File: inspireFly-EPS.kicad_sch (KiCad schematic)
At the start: 24 parts, among them J1 USB4085-GF-A_REVB, Q3 NMOS, Q4 NMOS, U1 STM32U575RIT6, U2 BQ25750RRVR, U3 TCAN332DCNR

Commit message: Good progress on BQ chip - need to do math later
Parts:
- added C14, C17: 80uF, symbol Device:C
- added C15, C16: 47nF, symbol Device:C
- added C18, C19: 100nF, symbol Device:C
- added C20: 470nF, symbol Device:C
- added C21, C22: 4.7uF, symbol Device:C
- added L1: L, symbol Device:L
- added Q10, Q5, Q6, Q7, Q8, Q9: NMOS, symbol Simulation_SPICE:NMOS
- added R10: 5.24k, symbol Device:R_US
- added R11: 30.31k, symbol Device:R_US
- added R12: 80k, symbol Device:R_US
- added R13: 3.3k, symbol Device:R_US
- added R14: 4.2k, symbol Device:R_US
- added R5: 5m, symbol Device:R_US
- added R6, R7: 10, symbol Device:R_US
- added R8: 250k, symbol Device:R_US
- added R9: 12k, symbol Device:R_US
- added TH1: Thermistor_US, symbol Device:Thermistor_US
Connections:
- net GND: now also U2.37 (EPAD), U2.8 (TS), C14.2, C17.2, C18.2, C19.1, C22.1, Q6.3 (S), Q8.3 (S), R10.2, R11.1, R11.2, R12.2, R13.1, R14.1, TH1.1, TH1.2
- net V_PROTECTED: now reaches R1.2, R3.1, R4.1
- net V_PROTECTED: now also U2.32 (SYS), C14.1, Q5.1 (D), Q9.1 (D)
- net at U2.10 (ILIM_HIZ): now also R13.2
- net at U2.11 (FBG): now also R9.2
- net at U2.12 (FB): now also R8.2, R9.1
- net at U2.13 (SRN): now also C19.2, C20.1, R7.1
- net at U2.14 (SRP): now also C18.1, C20.2, R6.1
- net at U2.15 (BATDRV): now also Q10.2 (G), Q9.2 (G)
- net at U2.16 (BATSRC): now also Q10.1 (D), Q9.3 (S)
- net at U2.18 (SW2): now also C16.2, L1.2, Q7.3 (S), Q8.1 (D)
- net at U2.19 (HIDRV2): now also Q7.2 (G)
- net at U2.20 (BTST2): now also C16.1
- net at U2.21 (LODRV2): now also Q8.2 (G)
- net +5V: now reaches U2.23 (DRV_SUP)
- net +5V: now also C22.2
- net at U2.24 (REGN): now also C21.1
- net at U2.25 (LODRV1): now also Q6.2 (G)
- net at U2.26 (BTST1): now also C15.1
- net at U2.27 (HIDRV1): now also Q5.2 (G)
- net at U2.28 (SW1): now also C15.2, L1.1, Q5.3 (S), Q6.1 (D)
- net at U2.36 (FSW_SYNC): now also R12.1
- net at U2.9 (ICHG): now also R14.2
- new net: C17.1, Q10.3 (S), Q7.1 (D), R5.1, R6.2
- new net BAT +: R5.2, R7.2, R8.1
- new net REGEN: C21.2, R10.1
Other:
- moved on the sheet: C10, C11, C12, C13, Q3, Q4, R1, R2, R3, R4, U2

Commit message: Changes to BQ Chip
Calculated some values, see overleaf doc. Adjusted presentation on schematic in regards to BQ chip. Also added battery holders
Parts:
- added BT1, BT2: BK-18650-PC4, BK-18650-PC4:BAT_BK-18650-PC4, symbol InspireFly-EPS-sym_lib:BK-18650-PC4
- added C23: ~, symbol Device:C
- added R15: 22.5k, symbol Device:R_US
- added R16: 1M, symbol Device:R_US
- added R17: 100k, symbol Device:R_US
- R8: value 250k -> 200k
- R9: value 12k -> 44.8k
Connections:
- net BAT +: now also BT1.1+, BT1.2+
- net GND: now also BT2.1-, BT2.2-, C23.2, R15.2; no longer U2.35 (ACOV)
- net V_BUS_COMBINED: now also C23.1, R16.1; no longer U2.34 (ACUV)
- net at C19.2, C20.1, R7.1: now also U2.14 (SRP); no longer U2.13 (SRN)
- net at C18.1, C20.2, R6.1: now also U2.13 (SRN); no longer U2.14 (SRP)
- new net: R15.1, R17.2, U2.35 (ACOV)
- new net: R16.2, R17.1, U2.34 (ACUV)
- new net: BT1.1-, BT1.2-, BT2.1+, BT2.2+
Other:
- moved on the sheet: C10, C11, C12, C13, C14, C15, C16, C17, C18, C19, C20, C21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

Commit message: More BQ work
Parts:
- L1: value L -> 2.2uH
- R1: value 2m -> 5m
- R12: value 80k -> 40k
- R14: value 4.2k -> 12.5k
- R15: value 22.5k -> 22.6k
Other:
- moved on the sheet: C13, C14
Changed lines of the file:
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@@
 	)
 	(junction
-		(at 347.98 261.62)
-		(diameter 0)
-		(color 0 0 0 0)
-	)
-	(junction
 		(at 250.19 91.44)
 		(diameter 0)
@@
 	)
 	(junction
-		(at 358.14 261.62)
-		(diameter 0)
-		(color 0 0 0 0)
-	)
-	(junction
 		(at 261.62 86.36)
 		(diameter 0)
@@
 	)
 	(junction
+		(at 349.25 261.62)
+		(diameter 0)
+		(color 0 0 0 0)
+	)
+	(junction
 		(at 260.35 91.44)
 		(diameter 0)
@@
 	)
 	(junction
+		(at 360.68 261.62)
+		(diameter 0)
+		(color 0 0 0 0)
+	)
+	(junction
 		(at 248.92 71.12)
 		(diameter 0)
@@
 	(wire
 		(pts
-			(xy 347.98 288.29) (xy 349.25 288.29)
-		)
-		(stroke
-			(width 0)
-			(type default)
-		)
-	)
-	(wire
-		(pts
 			(xy 124.46 317.5) (xy 124.46 323.85)
 		)
@@
 	(wire
 		(pts
-			(xy 327.66 276.86) (xy 327.66 279.4)
+			(xy 326.39 273.05) (xy 326.39 279.4)
 		)
 		(stroke
@@
 	(wire
 		(pts
-			(xy 347.98 288.29) (xy 347.98 261.62)
+			(xy 349.25 288.29) (xy 349.25 261.62)
 		)
 		(stroke
@@
 	(wire
 		(pts
-			(xy 347.98 261.62) (xy 358.14 261.62)
-		)
-		(stroke
-			(width 0)
-			(type default)
-		)
-	)
-	(wire
-		(pts
 			(xy 38.1 210.82) (xy 38.1 213.36)
 		)
@@
 	(wire
 		(pts
-			(xy 326.39 273.05) (xy 326.39 276.86)
-		)
-		(stroke
-			(width 0)
-			(type default)
-		)
-	)
-	(wire
-		(pts
 			(xy 318.77 302.26) (xy 312.42 302.26)
 		)
@@
 	(wire
 		(pts
+			(xy 349.25 261.62) (xy 360.68 261.62)
+		)
+		(stroke
+			(width 0)
+			(type default)
+		)
+	)
+	(wire
+		(pts
 			(xy 270.51 93.98) (xy 274.32 93.98)
 		)
@@
 	(wire
 		(pts
-			(xy 358.14 273.05) (xy 358.14 275.59)
+			(xy 360.68 273.05) (xy 360.68 276.86)
 		)
 		(stroke
@@
 	(wire
 		(pts
-			(xy 359.41 275.59) (xy 359.41 276.86)
-		)
-		(stroke
-			(width 0)
-			(type default)
-		)
-	)
-	(wire
-		(pts
 			(xy 257.81 68.58) (xy 274.32 68.58)
 		)
@@
 	(wire
 		(pts
-			(xy 358.14 275.59) (xy 359.41 275.59)
-		)
-		(stroke
-			(width 0)
-			(type default)
-		)
-	)
-	(wire
-		(pts
 			(xy 308.61 132.08) (xy 312.42 132.08)
 		)
@@
 	(wire
 		(pts
-			(xy 326.39 276.86) (xy 327.66 276.86)
-		)
-		(stroke
-			(width 0)
-			(type default)
-		)
-	)
-	(wire
-		(pts
 			(xy 236.22 86.36) (xy 248.92 86.36)
 		)
@@
 	(wire
 		(pts
-			(xy 358.14 261.62) (xy 372.11 261.62)
-		)
-		(stroke
-			(width 0)
-			(type default)
-		)
-	)
-	(wire
-		(pts
 			(xy 251.46 297.18) (xy 331.47 297.18)
 		)
@@
 	(wire
 		(pts
-			(xy 358.14 261.62) (xy 358.14 265.43)
+			(xy 360.68 261.62) (xy 360.68 265.43)
 		)
 		(stroke
@@
 	(wire
 		(pts
-			(xy 326.39 261.62) (xy 347.98 261.62)
+			(xy 326.39 261.62) (xy 349.25 261.62)
 		)
 		(stroke
@@
 	(wire
 		(pts
+			(xy 360.68 261.62) (xy 372.11 261.62)
+		)
+		(stroke
+			(width 0)
+			(type default)
+		)
+	)
+	(wire
+		(pts
 			(xy 276.86 317.5) (xy 261.62 317.5)
 		)
@@
 	(symbol
 		(lib_id "power:GND")
-		(at 327.66 287.02 0)
+		(at 326.39 287.02 0)
 		(unit 1)
 		(exclude_from_sim no)
@@
 		(fields_autoplaced yes)
 		(property "Reference" "#PWR016"
-			(at 327.66 293.37 0)
+			(at 326.39 293.37 0)
 			(effects
 				(font
@@
 		)
 		(property "Value" "GND"
-			(at 327.66 292.1 0)
+			(at 326.39 292.1 0)
 			(effects
 				(font
@@
 		)
 		(property "Footprint" ""
-			(at 327.66 287.02 0)
+			(at 326.39 287.02 0)
 			(effects
 				(font
@@
 		)
 		(property "Datasheet" ""
-			(at 327.66 287.02 0)
+			(at 326.39 287.02 0)
 			(effects
 				(font
@@
 		)
 		(property "Description" "Power symbol creates a global label with name \"GND\" , ground"
-			(at 327.66 287.02 0)
+			(at 326.39 287.02 0)
 			(effects
 				(font
@@
 	(symbol
 		(lib_id "Device:C")
-		(at 358.14 269.24 0)
+		(at 360.68 269.24 0)
 		(unit 1)
 		(exclude_from_sim no)
@@
 		(fields_autoplaced yes)
 		(property "Reference" "C14"
-			(at 361.95 267.9699 0)
+			(at 364.49 267.9699 0)
 			(effects
 				(font
@@
 		)
 		(property "Value" "80uF"
-			(at 361.95 270.5099 0)
+			(at 364.49 270.5099 0)
 			(effects
 				(font
@@
 		)
 		(property "Footprint" ""
-			(at 359.1052 273.05 0)
+			(at 361.6452 273.05 0)
 			(effects
 				(font
@@
 		)
 		(property "Datasheet" "~"
-			(at 358.14 269.24 0)
+			(at 360.68 269.24 0)
 			(effects
 				(font
@@
 		)
 		(property "Description" "Unpolarized capacitor"
-			(at 358.14 269.24 0)
+			(at 360.68 269.24 0)
 			(effects
 				(font
@@
 			)
 		)
-		(property "Value" "80k"
+		(property "Value" "40k"
 			(at 258.318 284.988 90)
 			(effects
@@
 			)
 		)
-		(property "Value" "22.5k"
+		(property "Value" "22.6k"
 			(at 275.59 287.0199 0)
 			(effects
@@
 			)
 		)
-		(property "Value" "2m"
+		(property "Value" "5m"
 			(at 307.34 257.81 90)
 			(effects
@@
 	(symbol
 		(lib_id "power:GND")
-		(at 359.41 276.86 0)
+		(at 360.68 276.86 0)
 		(unit 1)
 		(exclude_from_sim no)
@@
 		(fields_autoplaced yes)
 		(property "Reference" "#PWR019"
-			(at 359.41 283.21 0)
+			(at 360.68 283.21 0)
 			(effects
 				(font
@@
 		)
 		(property "Value" "GND"
-			(at 359.41 281.94 0)
+			(at 360.68 281.94 0)
 			(effects
 				(font
@@
 		)
 		(property "Footprint" ""
-			(at 359.41 276.86 0)
+			(at 360.68 276.86 0)
 			(effects
 				(font
@@
 		)
 		(property "Datasheet" ""
-			(at 359.41 276.86 0)
+			(at 360.68 276.86 0)
 			(effects
 				(font
@@
 		)
 		(property "Description" "Power symbol creates a global label with name \"GND\" , ground"
-			(at 359.41 276.86 0)
+			(at 360.68 276.86 0)
 			(effects
 				(font
@@
 			)
 		)
-		(property "Value" "4.2k"
+		(property "Value" "12.5k"
 			(at 190.754 303.784 90)
 			(effects
@@
 			)
 		)
-		(property "Value" "L"
+		(property "Value" "2.2uH"
 			(at 361.95 299.72 90)
 			(effects
@@
 	(symbol
 		(lib_id "Device:C")
-		(at 327.66 283.21 0)
+		(at 326.39 283.21 0)
 		(unit 1)
 		(exclude_from_sim no)
@@
 		(fields_autoplaced yes)
 		(property "Reference" "C13"
-			(at 331.47 281.9399 0)
+			(at 330.2 281.9399 0)
 			(effects
 				(font
@@
 		)
 		(property "Value" "2.2uF"
-			(at 331.47 284.4799 0)
+			(at 330.2 284.4799 0)
 			(effects
 				(font
@@
 		)
 		(property "Footprint" ""
-			(at 328.6252 287.02 0)
+			(at 327.3552 287.02 0)
 			(effects
 				(font
@@
 		)
 		(property "Datasheet" "~"
-			(at 327.66 283.21 0)
+			(at 326.39 283.21 0)
 			(effects
 				(font
@@
 		)
 		(property "Description" "Unpolarized capacitor"
-			(at 327.66 283.21 0)
+			(at 326.39 283.21 0)
 			(effects
 				(font

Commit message: Updates to BQ chip and routing
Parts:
- added D1: LED, Diode_SMD:D_0805_2012Metric_Pad1.15x1.40mm_HandSolder, symbol Device:LED
- added J2: Conn_01x02_Pin, Connector_PinSocket_2.54mm:PinSocket_1x02_P2.54mm_Vertical, symbol Connector:Conn_01x02_Pin
- added R18, R19: 10k, Resistor_SMD:R_0402_1005Metric_Pad0.72x0.64mm_HandSolder, symbol Device:R_US
- added R20: 330, Resistor_SMD:R_0402_1005Metric_Pad0.72x0.64mm_HandSolder, symbol Device:R_US
- added R21: 10K, Resistor_SMD:R_0402_1005Metric_Pad0.72x0.64mm_HandSolder, symbol Device:R_US
- BT1, BT2: footprint BK-18650-PC4:BAT_BK-18650-PC4 -> inspireFly-EPS-footprints:BAT_BK-18650-PC4
- C1, C13, C15, C16, C18, C19, C2, C20, C21, C22, C3, C4, C5, C6, C7, C8, C9: footprint (none) -> Capacitor_SMD:C_0402_1005Metric_Pad0.74x0.62mm_HandSolder
- C10, C11: footprint (none) -> Capacitor_SMD:C_0805_2012Metric_Pad1.18x1.45mm_HandSolder
- C12: footprint (none) -> Capacitor_SMD:C_1206_3216Metric_Pad1.33x1.80mm_HandSolder
- C14, C17: value 80uF -> 47uF; footprint (none) -> inspireFly-EPS-footprints:CAP_EEEFN1J470L
- C23: value ~ -> 2.2uF; footprint (none) -> Capacitor_SMD:C_1206_3216Metric_Pad1.33x1.80mm_HandSolder
- J1: footprint USB4085-GF-A_REVB:GCT_USB4085-GF-A_REVB -> inspireFly-EPS-footprints:GCT_USB4085-GF-A_REVB
- L1: footprint (none) -> inspireFly-EPS-footprints:WE-MXGI_4020
- Q10, Q3, Q4, Q5, Q6, Q7, Q8, Q9: value NMOS -> SQJA62EP-T1_GE3; footprint (none) -> inspireFly-EPS-footprints:TRANS_SQJA62EP-T1_GE3
- R1, R4, R5: footprint (none) -> Resistor_SMD:R_1206_3216Metric_Pad1.30x1.75mm_HandSolder
- R10, R11, R12, R13, R14, R15, R16, R17, R8, R9, TR1: footprint (none) -> Resistor_SMD:R_0402_1005Metric_Pad0.72x0.64mm_HandSolder
- R2, R3, R6, R7: footprint (none) -> Resistor_SMD:R_0603_1608Metric_Pad0.98x0.95mm_HandSolder
- U1: footprint LQFP64-10x10mm_STM -> inspireFly-EPS-footprints:LQFP64-10x10mm_STM
- U2: footprint VQFN36_RRV_TEX -> inspireFly-EPS-footprints:VQFN36_RRV_TEX
- U3: footprint DCN0008A_N -> Package_TO_SOT_SMD:SOT-23-8
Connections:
- net V_BUS_COMBINED is gone; now on net USB_V: C23.1, Q3.1 (D), R16.1, U2.33 (VAC)
- net +3.3V: now also R18.2, R19.2, R21.1
- net GND: now also U2.7 (*CE), D1.1 (K), J2.2 (Pin_2)
- net USB_V: now also J2.1 (Pin_1)
- net I2C3-SCL: now reaches U1.8 (PC0)
- net I2C3-SCL: now also U2.2 (SDA), R18.1
- net I2C3-SDA: now reaches U1.9 (PC1)
- net I2C3-SDA: now also U2.1 (SCL), R19.1
- net POWER_GOOD: now reaches U2.6 (*PG)
- net POWER_GOOD: now also R20.1, R21.2
- new net: D1.2 (A), R20.2
- no-connect marks 6 -> 9
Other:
- moved on the sheet: C12, C14, C17

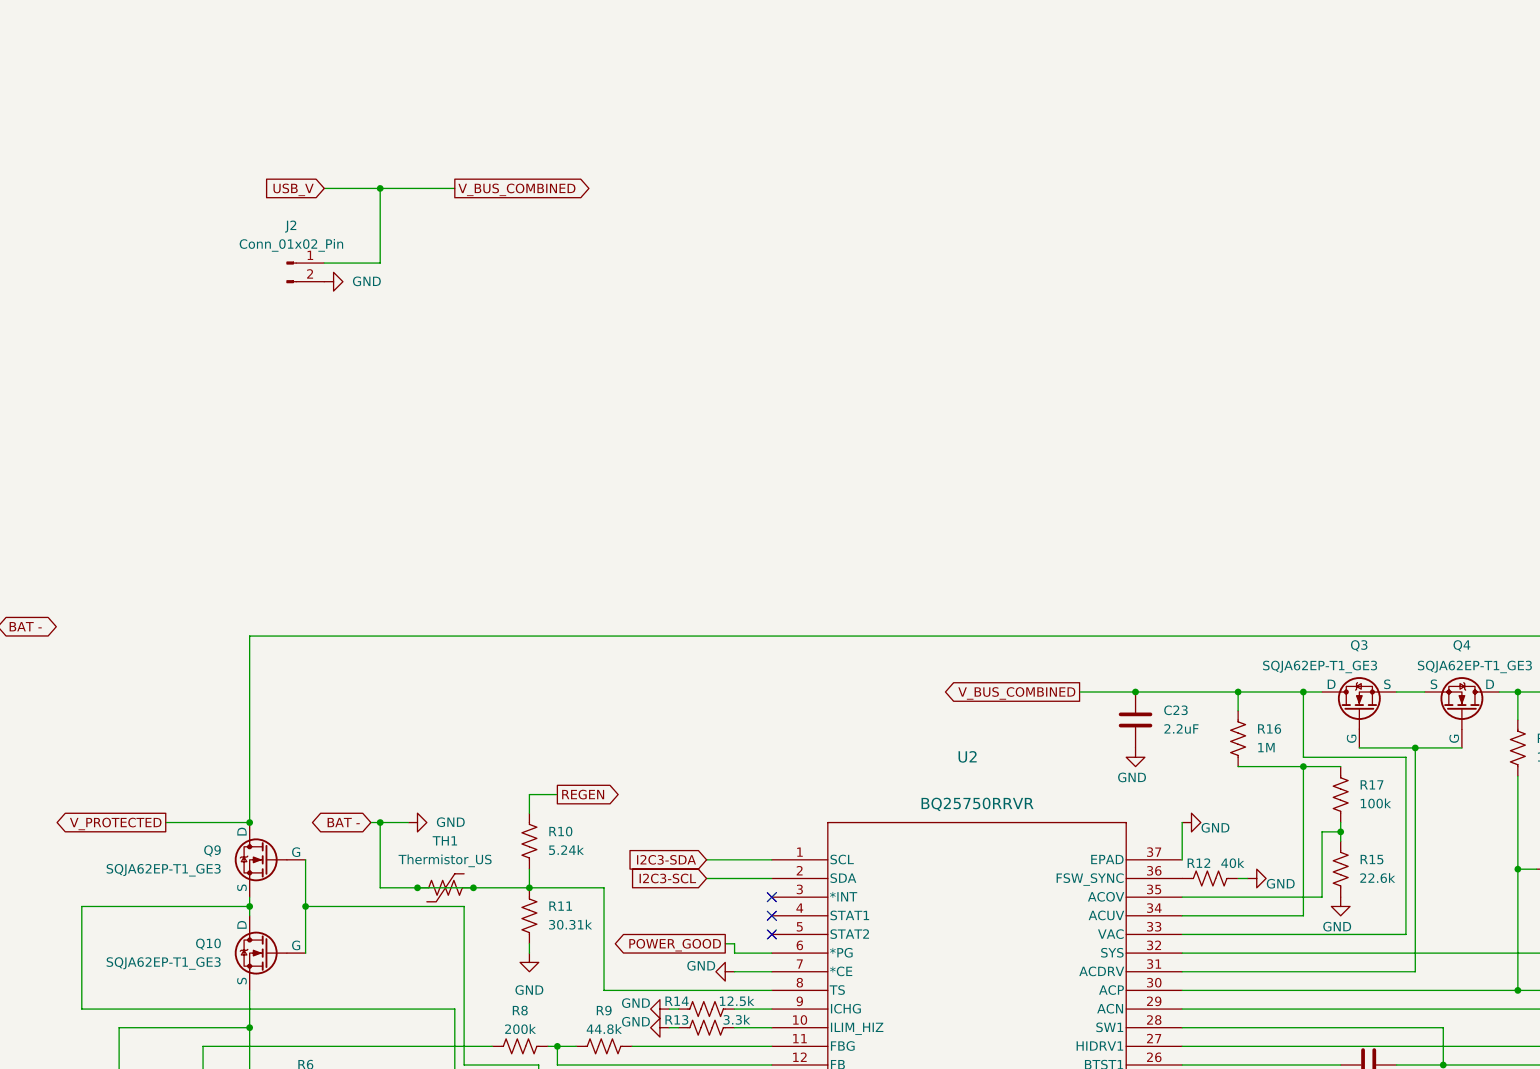
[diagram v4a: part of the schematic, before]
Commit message: Added diode to USB
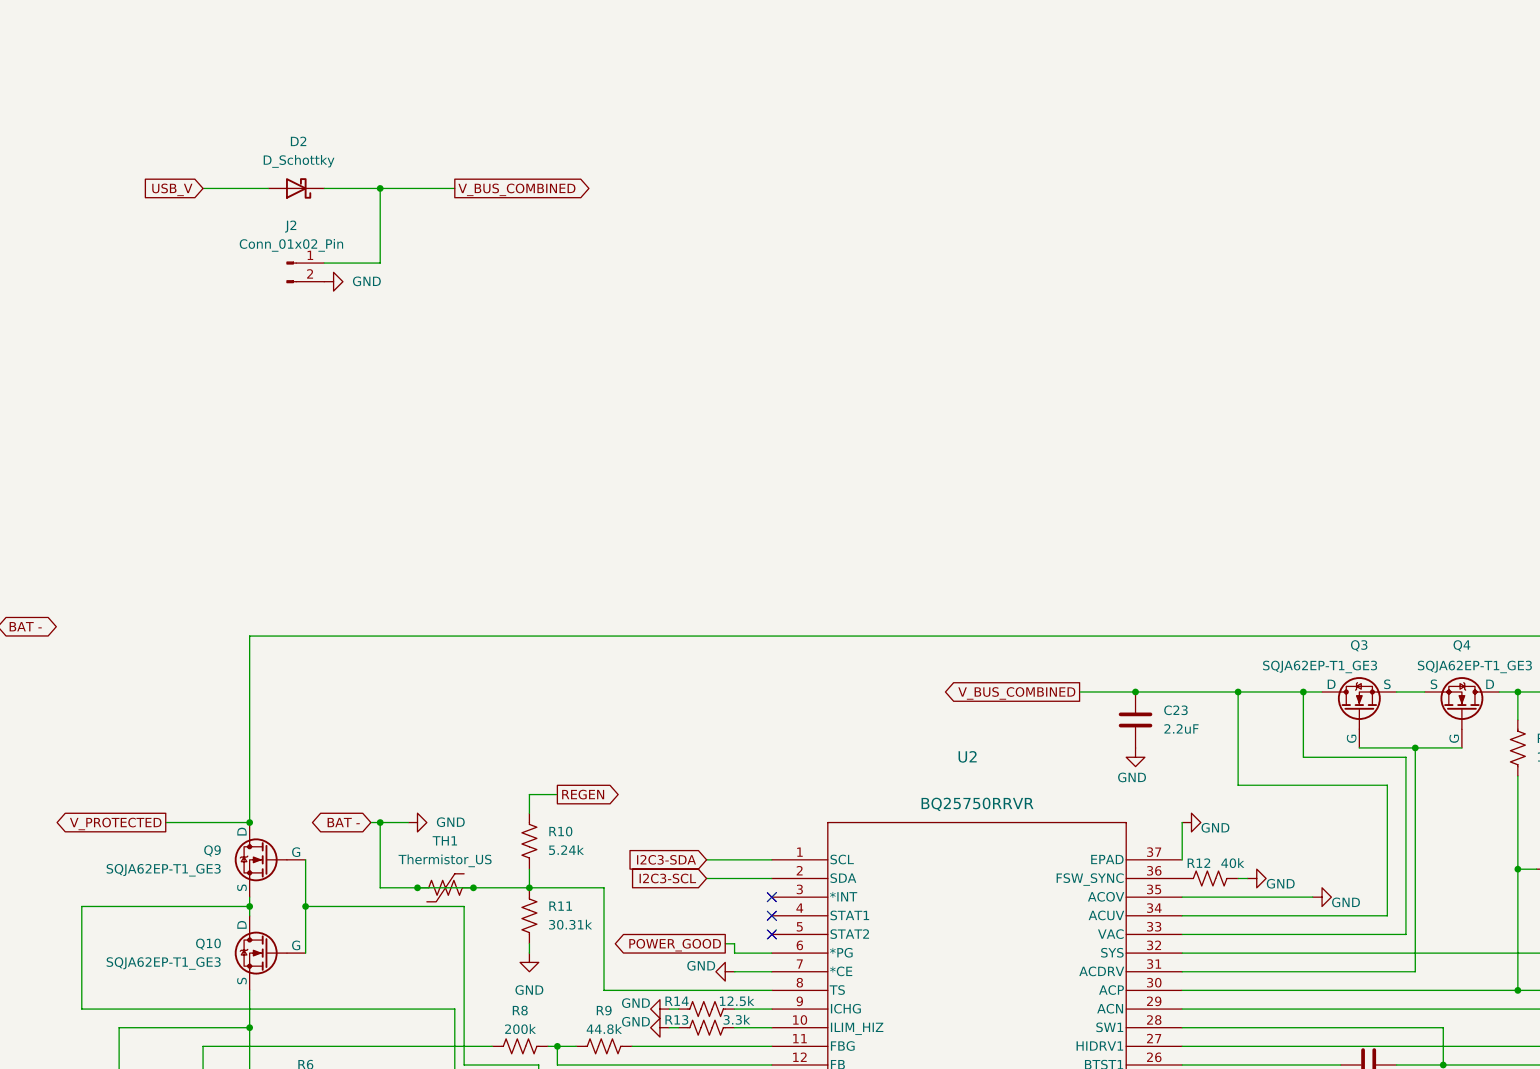
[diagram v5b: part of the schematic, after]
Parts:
- removed R15: 22.6k, Resistor_SMD:R_0402_1005Metric_Pad0.72x0.64mm_HandSolder, symbol Device:R_US
- removed R16: 1M, Resistor_SMD:R_0402_1005Metric_Pad0.72x0.64mm_HandSolder, symbol Device:R_US
- removed R17: 100k, Resistor_SMD:R_0402_1005Metric_Pad0.72x0.64mm_HandSolder, symbol Device:R_US
- added D2: D_Schottky, inspireFly-EPS-footprints:SDT5A60SA13, symbol Device:D_Schottky
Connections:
- net GND: now also U2.35 (ACOV)
- net USB_V: now also D2.2 (A); no longer C23.1, J2.1 (Pin_1), Q3.1 (D), U2.33 (VAC)
- net V_BUS_COMBINED: now reaches U2.34 (ACUV)
- net V_BUS_COMBINED: now also C23.1, J2.1 (Pin_1), Q3.1 (D), U2.33 (VAC), D2.1 (K)

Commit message: Added INAs
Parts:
- added C24, C25, C26, C27, C28, C29: 100nF, Capacitor_SMD:C_0402_1005Metric_Pad0.74x0.62mm_HandSolder, symbol Device:C
- added R15, R16, R23: 5m, Resistor_SMD:R_1206_3216Metric_Pad1.30x1.75mm_HandSolder, symbol Device:R_US
- added R17, R22, R24: 10, Resistor_SMD:R_0603_1608Metric_Pad0.98x0.95mm_HandSolder, symbol Device:R_US
- added U5, U6, U7: INA180A3IDBVT, inspireFly-EPS-footprints:SOT95P280X145-5N, symbol InspireFly-EPS-sym_lib:INA180A3IDBVT
- D2: value D_Schottky -> SDT5A60SA
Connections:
- net +3.3V: now also C24.1, C25.1, C28.1, R15.2, U5.4 (IN-), U5.5 (VS), U6.5 (VS), U7.5 (VS)
- net +5V: now also R16.2, U6.4 (IN-)
- net GND: now also C24.2, C25.2, C26.2, C27.2, C28.2, C29.2, U5.2 (GND), U6.2 (GND), U7.2 (GND)
- net ADC1_IN3: now reaches U1.10 (PC2)
- net ADC1_IN3: now also C26.1, R17.2
- net ADC1_IN4: now reaches U1.11 (PC3)
- net ADC1_IN4: now also C27.1, R22.2
- net ADC1_IN5: now reaches U1.14 (PA0)
- net ADC1_IN5: now also C29.1, R24.2
- new net: R22.1, U6.1 (OUT)
- new net: R15.1, U5.3 (IN+)
- new net: R17.1, U5.1 (OUT)
- new net: R16.1, U6.3 (IN+)
- new net: R24.1, U7.1 (OUT)
- new net SUPERCAP_LOAD/SLOWCHARGE: R23.2, U7.4 (IN-)
- new net SUPERCAP_OUT: R23.1, U7.3 (IN+)
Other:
- note added: "3.3V Regulator"
- note added: "5V Regulator"
- note added: "Battery Management"
- note added: "CAN"
- note added: "Microproccesor"
- note added: "Misc."
- note added: "SuperCap Array & Regulator"
- note added: "USB-C"
- moved on the sheet: BT1, BT2, C1, C10, C11, C12, C13, C14, C15, C16, C17, C18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
